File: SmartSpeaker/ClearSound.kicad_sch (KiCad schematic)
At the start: 60 parts

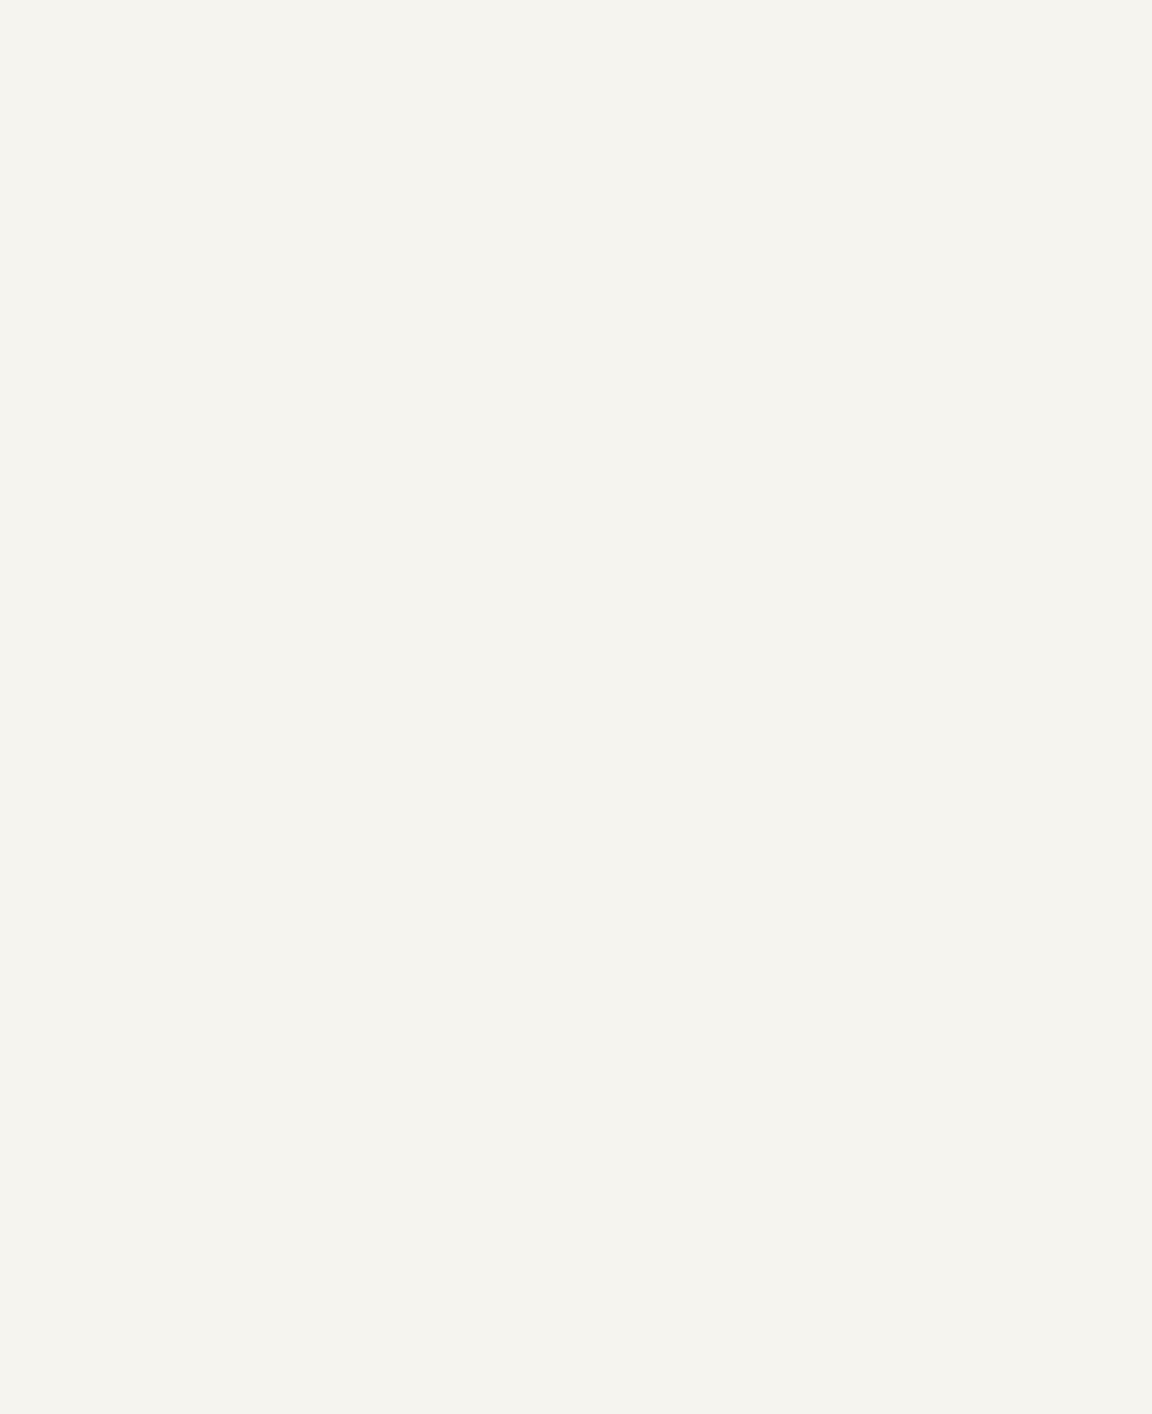
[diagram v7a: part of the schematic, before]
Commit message: add power regulator for dsp
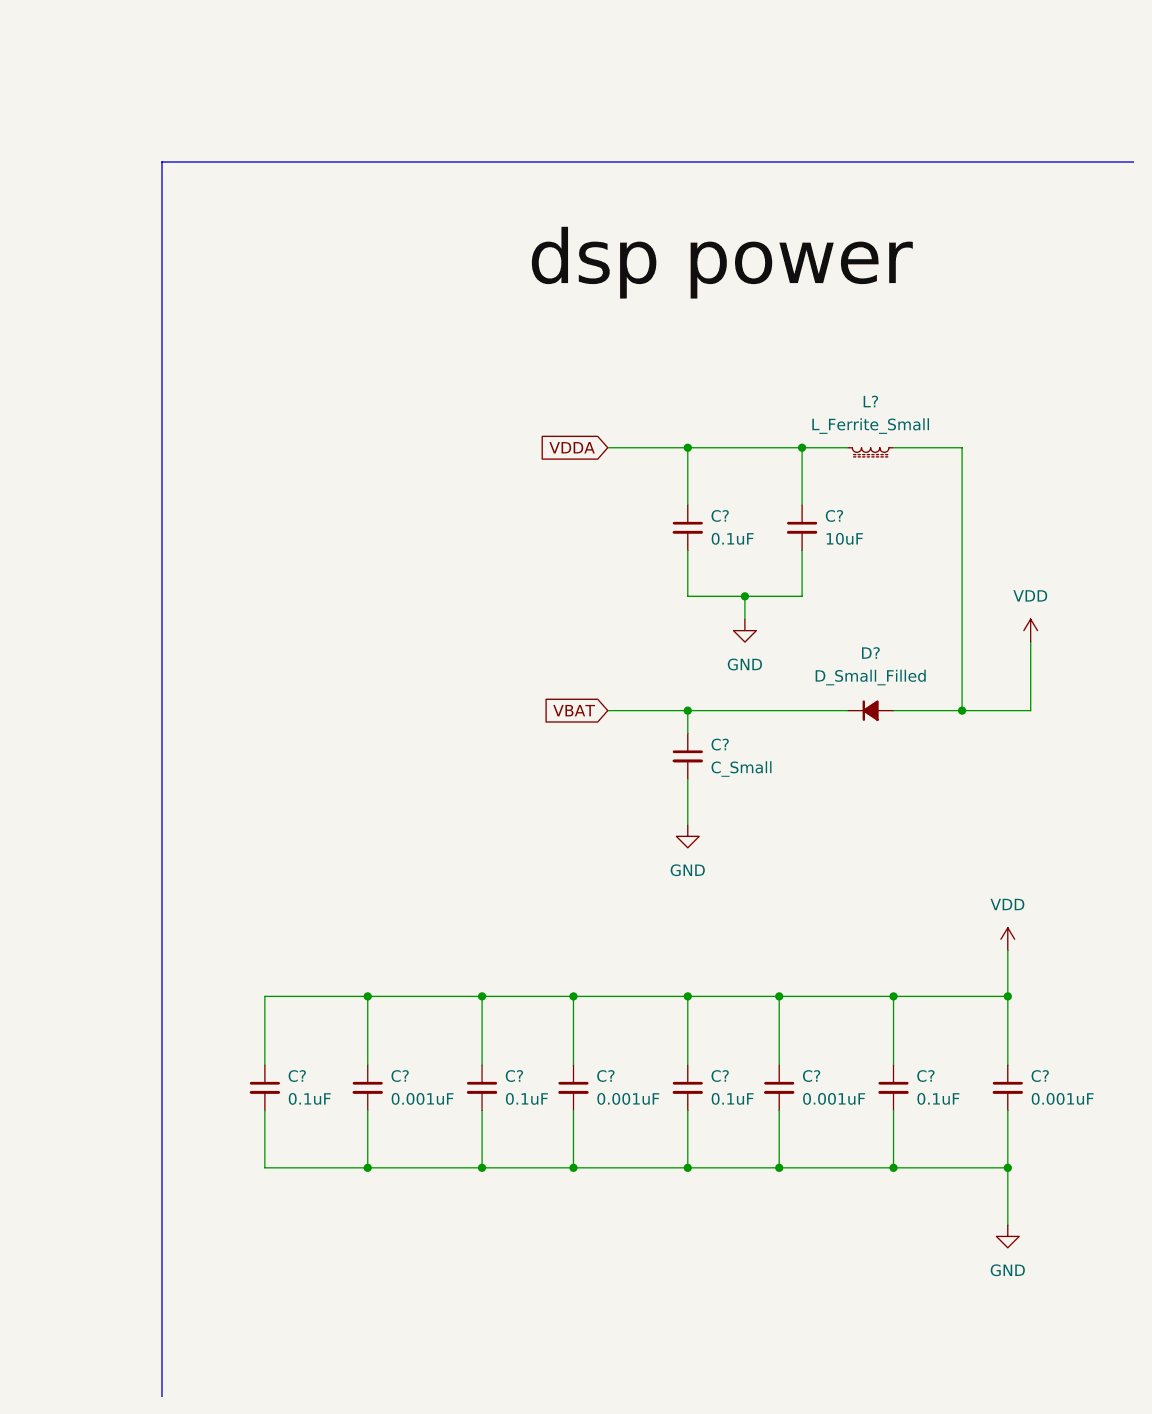
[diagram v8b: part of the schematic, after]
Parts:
- added C?: C_Small, Capacitor_SMD:C_0402_1005Metric, symbol Device:C_Small
- added C? (x4): 0.001uF, Capacitor_SMD:C_0402_1005Metric, symbol Device:C_Small
- added C? (x5): 0.1uF, Capacitor_SMD:C_0402_1005Metric, symbol Device:C_Small
- added C?: 10uF, Capacitor_SMD:C_0402_1005Metric, symbol Device:C_Small
- added D?: D_Small_Filled, Diode_SMD:D_0805_2012Metric, symbol Device:D_Small_Filled
- added L?: L_Ferrite_Small, Inductor_SMD:L_6.3x6.3_H3, symbol Device:L_Ferrite_Small
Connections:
- net GND: now also C?.2, C?.2, C?.2, C?.2, C?.2, C?.2, C?.2, C?.2, C?.2, C?.2, C?.2
- net VDD: now also C?.1, C?.1, C?.1, C?.1, C?.1, C?.1, C?.1, C?.1, D?.2 (A), L?.1
- net VDDA: now also C?.1, C?.1, L?.2
- new net VBAT: C?.1, D?.1 (K)
